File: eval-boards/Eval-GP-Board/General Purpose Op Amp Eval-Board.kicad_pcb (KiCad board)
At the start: 2 copper layers, 40 parts, among them J1 IN, J2 Conn_01x03_Male, J3 OUT, J4 TP1, J5 TP2, J6 TP3, J7 TP4, J8 TP5, J9 TP6, U1 ADA4522-1, U2 OPA847xD, U3 ADA4807-1

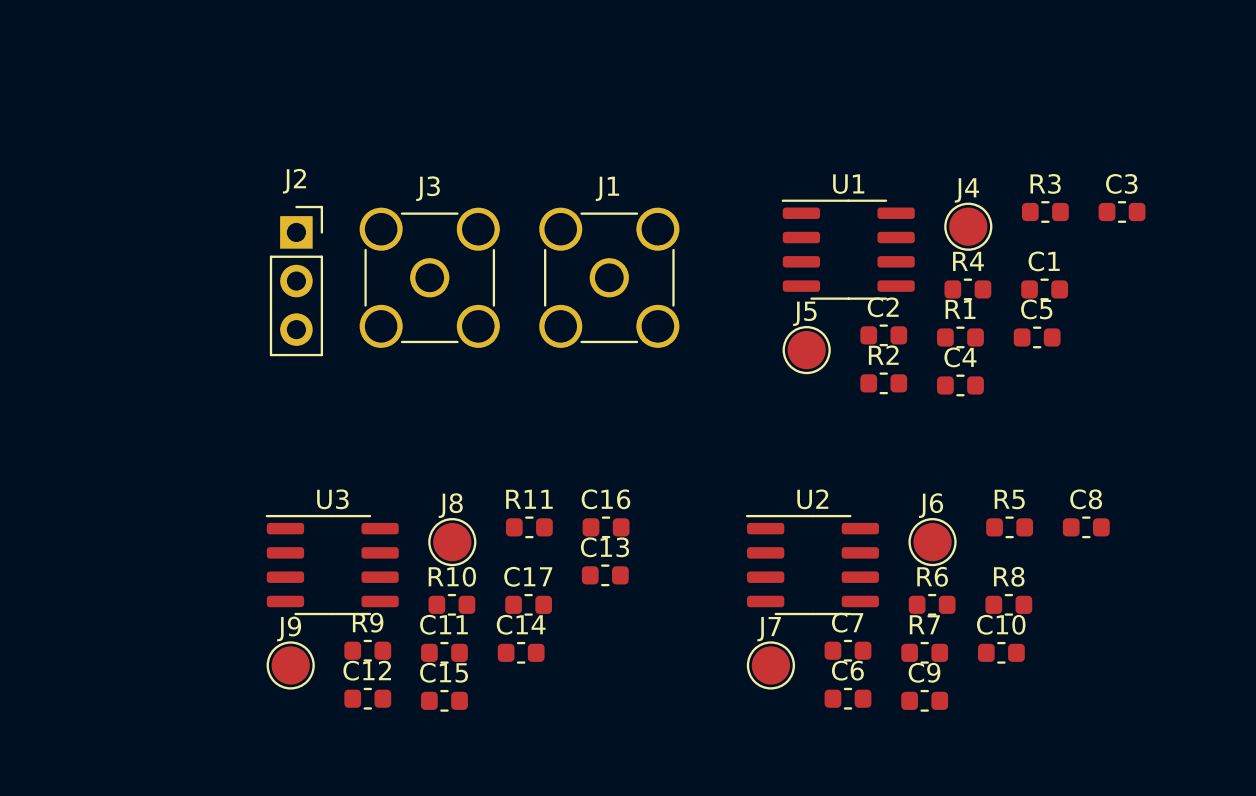
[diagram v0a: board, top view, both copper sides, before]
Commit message: Updated schematic
均采用双运放，前级4522可以单运放工作也可以级联工作
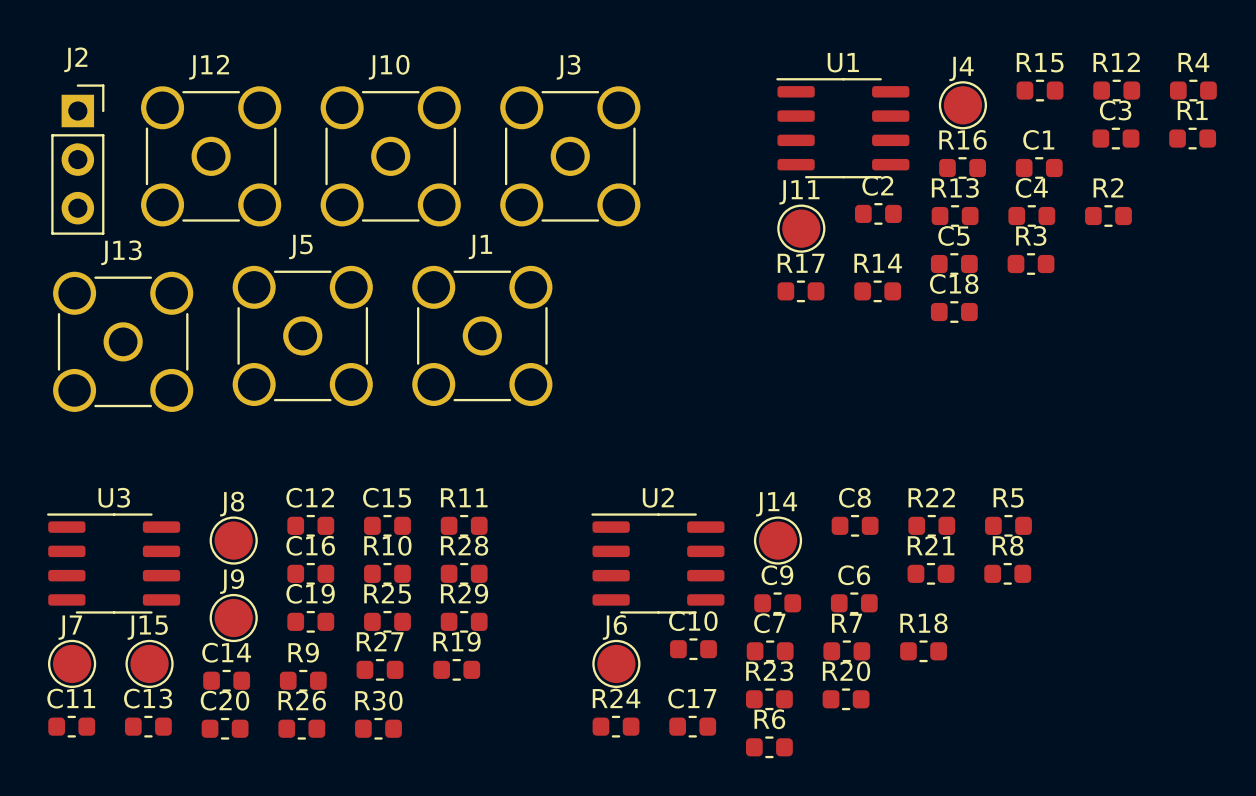
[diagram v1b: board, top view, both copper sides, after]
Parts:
- added C18: C, Capacitor_SMD:C_0603_1608Metric, F.Cu at (167.0, 98.7)
- added C19: C, Capacitor_SMD:C_0603_1608Metric, F.Cu at (133.4, 114.9)
- added C20: C, Capacitor_SMD:C_0603_1608Metric, F.Cu at (128.9, 120.5)
- added J10: OUT_B, Connector_Coaxial:SMA_Amphenol_901-144_Vertical, F.Cu at (137.6, 90.6)
- added J11: TP2, TestPoint:TestPoint_Pad_D2.0mm, F.Cu at (159.0, 94.3)
- added J12: IN_B, Connector_Coaxial:SMA_Amphenol_901-144_Vertical, F.Cu at (128.2, 90.6)
- added J13: OUT_B, Connector_Coaxial:SMA_Amphenol_901-144_Vertical, F.Cu at (123.6, 100.3)
- added J14: TP4, TestPoint:TestPoint_Pad_D2.0mm, F.Cu at (157.8, 110.6)
- added J15: TP8, TestPoint:TestPoint_Pad_D2.0mm, F.Cu at (125.0, 117.1)
- added R12: R, Resistor_SMD:R_0603_1608Metric, F.Cu at (175.5, 87.1)
- added R13: R, Resistor_SMD:R_0603_1608Metric, F.Cu at (167.1, 93.7)
- added R14: R, Resistor_SMD:R_0603_1608Metric, F.Cu at (163.0, 97.6)
- added R15: R, Resistor_SMD:R_0603_1608Metric, F.Cu at (171.5, 87.1)
- added R16: R, Resistor_SMD:R_0603_1608Metric, F.Cu at (167.5, 91.2)
- added R17: R, Resistor_SMD:R_0603_1608Metric, F.Cu at (159.0, 97.6)
- added R18: R, Resistor_SMD:R_0603_1608Metric, F.Cu at (165.4, 116.4)
- added R19: R, Resistor_SMD:R_0603_1608Metric, F.Cu at (141.0, 117.4)
- added R20: R, Resistor_SMD:R_0603_1608Metric, F.Cu at (161.4, 118.9)
- added R21: R, Resistor_SMD:R_0603_1608Metric, F.Cu at (165.8, 112.4)
- added R22: R, Resistor_SMD:R_0603_1608Metric, F.Cu at (165.9, 109.9)
- added R23: R, Resistor_SMD:R_0603_1608Metric, F.Cu at (157.4, 118.9)
- added R24: R, Resistor_SMD:R_0603_1608Metric, F.Cu at (149.3, 120.4)
- added R25: R, Resistor_SMD:R_0603_1608Metric, F.Cu at (137.4, 114.9)
- added R26: R, Resistor_SMD:R_0603_1608Metric, F.Cu at (132.9, 120.5)
- added R27: R, Resistor_SMD:R_0603_1608Metric, F.Cu at (137.0, 117.4)
- added R28: R, Resistor_SMD:R_0603_1608Metric, F.Cu at (141.4, 112.4)
- added R29: R, Resistor_SMD:R_0603_1608Metric, F.Cu at (141.4, 114.9)
- added R30: R, Resistor_SMD:R_0603_1608Metric, F.Cu at (136.9, 120.5)
- J1: value IN -> IN_A
- J3: value OUT -> OUT_A
- J5: value TP2 -> OUT_A; footprint TestPoint:TestPoint_Pad_D2.0mm -> Connector_Coaxial:SMA_Amphenol_901-144_Vertical
- J7: value TP4 -> TP6
- J9: value TP6 -> TP7
- U1: value ADA4522-1 -> ADA4522-2
- U2: value OPA847xD -> ADA4075-2
- U3: value ADA4807-1 -> ADA4807-2ARM
- moved J7 36.5 mm to (120.9, 117.1)
- moved J5 26.4 mm to (133.0, 99.9)
- moved C13 25.2 mm to (124.9, 120.4)
- moved C11 19.9 mm to (120.9, 120.4)
- moved J6 17.7 mm to (149.4, 117.1)
- moved C10 16.1 mm to (153.4, 116.3)
- moved R1 16.0 mm to (179.5, 89.6)
- moved R4 15.7 mm to (179.5, 87.1)
- moved C16 15.6 mm to (133.4, 112.4)
- moved C14 15.5 mm to (129.0, 118.0)
- moved R2 14.7 mm to (175.1, 93.7)
- moved J2 13.1 mm to (121.2, 88.2)
- moved C8 12.1 mm to (161.8, 109.9)
- moved J8 11.4 mm to (129.4, 110.6)
- moved U3 11.4 mm to (123.1, 111.8)
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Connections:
- net /Low noise amplifier/OUT renamed /Low noise amplifier/OUT_A
- C1 pad 1: /VEE -> /VCC
- C10 pad 1: /High gain amplifier/OUT -> /High gain amplifier/OUT_A
- C15 pad 1: /Second order filtering/OUT -> Net-(C15-Pad1)
- C17 pad 1: /Second order filtering/OUT -> /High gain amplifier/OUT_B
- C2 pad 1: /VEE -> /VCC
- C3 pad 1: /VCC -> /VEE
- C4 pad 1: /VCC -> /VEE
- J1 pad 1: /Low noise amplifier/signal_in -> /Low noise amplifier/signal_in_A
- J3 pad 1: /Second order filtering/OUT -> /Second order filtering/OUT_A
- J4 pad 1: /Low noise amplifier/signal_in -> /Low noise amplifier/signal_in_A
- J7 pad 1: /High gain amplifier/OUT -> /High gain amplifier/OUT_B
- J8 pad 1: /High gain amplifier/OUT -> /High gain amplifier/OUT_A
- J9 pad 1: /Second order filtering/OUT -> /Second order filtering/OUT_A
- R1 pad 1: /Low noise amplifier/signal_in -> Net-(R1-Pad1)
- R1 pad 2: GND -> Net-(R1-Pad2)
- R11 pad 1: /Second order filtering/OUT -> Net-(R11-Pad1)
- R11 pad 2: Net-(C17-Pad2) -> Net-(C15-Pad1)
- R2 pad 1: Net-(R2-Pad1) -> /Low noise amplifier/signal_in_A
- R2 pad 2: /Low noise amplifier/signal_in -> GND
- R3 pad 1: Net-(R2-Pad1) -> Net-(R3-Pad1)
- R3 pad 2: GND -> /Low noise amplifier/signal_in_A
- R4 pad 1: Net-(C5-Pad2) -> Net-(R3-Pad1)
- R4 pad 2: Net-(R4-Pad2) -> GND
- R6 pad 1: Net-(C10-Pad2) -> Net-(R18-Pad2)
- R9 pad 2: /High gain amplifier/OUT -> /High gain amplifier/OUT_A
- U1 pad 1: (no net) -> Net-(R1-Pad2)
- U1 pad 2: Net-(R4-Pad2) -> Net-(R1-Pad1)
- U1 pad 3: Net-(R2-Pad1) -> Net-(R3-Pad1)
- U1 pad 5: (no net) -> Net-(R13-Pad1)
- U1 pad 6: Net-(C5-Pad2) -> Net-(R17-Pad2)
- U1 pad 7: /VCC -> Net-(R14-Pad1)
- U1 pad 8: (no net) -> /VCC
- U2 pad 1: (no net) -> Net-(R18-Pad2)
- U2 pad 5: (no net) -> Net-(R21-Pad1)
- U2 pad 6: Net-(C10-Pad2) -> Net-(R23-Pad2)
- U2 pad 7: /VCC -> Net-(R23-Pad1)
- U2 pad 8: (no net) -> /VCC
- U3 pad 1: /Second order filtering/OUT -> Net-(C15-Pad1)
- U3 pad 2: /VEE -> Net-(R11-Pad1)
- U3 pad 4: Net-(C17-Pad2) -> /VEE
- U3 pad 5: (no net) -> Net-(C19-Pad1)
- U3 pad 6: /VCC -> Net-(R27-Pad1)
- U3 pad 7: (no net) -> Net-(C20-Pad1)
- U3 pad 8: (no net) -> /VCC

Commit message: first edition PCB
复杂度有点高。。。画的有点晕，问题很大
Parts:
- moved R2 120.9 mm to (55.9, 73.7), turned to 90 degrees
- moved R4 120.6 mm to (59.7, 73.7), turned to 90 degrees
- moved J4 117.2 mm to (52.1, 67.3)
- moved C1 113.8 mm to (57.6, 91.4)
- moved R1 113.0 mm to (67.3, 75.7), turned to 90 degrees
- moved C6 110.0 mm to (57.1, 80.0)
- moved C3 109.5 mm to (66.0, 86.4), turned to 180 degrees
- moved R12 109.4 mm to (67.3, 71.1), turned to 270 degrees
- moved R3 109.2 mm to (63.5, 77.5), turned to 180 degrees
- moved C4 106.8 mm to (64.8, 83.0), turned to 270 degrees
- moved C2 106.1 mm to (57.1, 87.6)
- moved C7 105.0 mm to (57.1, 85.1)
- moved C5 103.8 mm to (67.3, 67.3), turned to 270 degrees
- moved J1 99.4 mm to (52.1, 58.4)
- moved C8 97.1 mm to (66.0, 94.0), turned to 180 degrees
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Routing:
- net GND: track 0.00 -> 164.1 mm, vias 0 -> 2
- net /VCC: track 0.00 -> 119.7 mm, vias 0 -> 4
- net /VEE: track 0.00 -> 83.5 mm, vias 0 -> 4
- net /Low noise amplifier/OUT_A: track 0.00 -> 52.5 mm, vias 0 -> 4
- net /Low noise amplifier/signal_in_B: track 0.00 -> 45.1 mm, vias 0 -> 2
- net /Second order filtering/OUT_A: track 0.00 -> 42.0 mm, vias 0 -> 2
- net /Low noise amplifier/signal_in_A: track 0.00 -> 26.0 mm, vias 0 -> 2
- net /High gain amplifier/OUT_A: track 0.00 -> 24.9 mm, vias 0 -> 2
- net /Second order filtering/OUT_B: track 0.00 -> 20.1 mm
- net Net-(R11-Pad1): track 0.00 -> 18.2 mm
- net Net-(C14-Pad2): track 0.00 -> 18.1 mm, vias 0 -> 2
- net /High gain amplifier/OUT_B: track 0.00 -> 17.0 mm, vias 0 -> 2
- net Net-(C19-Pad1): track 0.00 -> 14.3 mm
- net Net-(C20-Pad2): track 0.00 -> 14.0 mm
- net Net-(C20-Pad1): track 0.00 -> 13.9 mm
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
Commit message: update-version
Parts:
- renumbered J1 to IN_A, J12 to IN_B, J3 to OUT_A, J5 to OUT_A, J10 to OUT_B, J13 to OUT_B, J4 to TP1, J11 to TP2, J6 to TP3, J14 to TP4, J8 to TP5, J7 to TP6, J9 to TP7, J15 to TP8
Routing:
- net /Second order filtering/OUT_A: track 42.0 -> 40.9 mm
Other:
- board outline added: 81.3 x 53.3 mm
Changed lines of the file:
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@@
   (general
     (thickness 1.6)
-    (drawings 4)
-    (tracks 297)
+    (drawings 8)
+    (tracks 298)
     (zones 0)
     (modules 68)
@@
   )
   (setup
-    (last_trace_width 0.4)
+    (last_trace_width 0.25)
     (user_trace_width 0.4)
     (trace_clearance 0.2)
@@
     (tags capacitor)
     (attr smd)
-    (fp_text reference C9 (at 0 -1.43) (layer F.SilkS)
+    (fp_text reference C9 (at 0 -1.27) (layer F.SilkS)
       (effects (font (size 1 1) (thickness 0.15)))
     )
@@
     (tags capacitor)
     (attr smd)
-    (fp_text reference C13 (at 0 -1.43) (layer F.SilkS)
+    (fp_text reference C13 (at 0 1.27) (layer F.SilkS)
       (effects (font (size 1 1) (thickness 0.15)))
     )
@@
     (descr https://www.amphenolrf.com/downloads/dl/file/id/7023/product/3103/901_144_customer_drawing.pdf)
     (tags "SMA THT Female Jack Vertical")
-    (fp_text reference J1 (at 0 -4.75) (layer F.SilkS)
+    (fp_text reference IN_A (at 0 -5.08) (layer F.SilkS)
       (effects (font (size 1 1) (thickness 0.15)))
     )
@@
     (descr https://www.amphenolrf.com/downloads/dl/file/id/7023/product/3103/901_144_customer_drawing.pdf)
     (tags "SMA THT Female Jack Vertical")
-    (fp_text reference J3 (at 0 -4.75) (layer F.SilkS)
+    (fp_text reference OUT_A (at 0 -4.75) (layer F.SilkS)
       (effects (font (size 1 1) (thickness 0.15)))
     )
@@
     (tags "test point SMD pad")
     (attr virtual)
-    (fp_text reference J4 (at 0 -1.998) (layer F.SilkS)
+    (fp_text reference TP1 (at -3.81 0) (layer F.SilkS)
       (effects (font (size 1 1) (thickness 0.15)))
     )
@@
     (fp_circle (center 0 0) (end 0 1.2) (layer F.SilkS) (width 0.12))
     (fp_circle (center 0 0) (end 1.5 0) (layer F.CrtYd) (width 0.05))
-    (fp_text user %R (at 0 -2) (layer F.Fab)
-      (effects (font (size 1 1) (thickness 0.15)))
-    )
     (pad 1 smd circle (at 0 0) (size 2 2) (layers F.Cu F.Mask)
       (net 20 "/Low noise amplifier/signal_in_A"))
@@
     (descr https://www.amphenolrf.com/downloads/dl/file/id/7023/product/3103/901_144_customer_drawing.pdf)
     (tags "SMA THT Female Jack Vertical")
-    (fp_text reference J5 (at 0 -4.75) (layer F.SilkS)
+    (fp_text reference OUT_A (at 0 -4.75) (layer F.SilkS)
       (effects (font (size 1 1) (thickness 0.15)))
     )
@@
     (tags "test point SMD pad")
     (attr virtual)
-    (fp_text reference J6 (at 0 -1.998) (layer F.SilkS)
+    (fp_text reference TP3 (at 0 -1.998) (layer F.SilkS)
       (effects (font (size 1 1) (thickness 0.15)))
     )
@@
     (tags "test point SMD pad")
     (attr virtual)
-    (fp_text reference J7 (at 0 -1.998) (layer F.SilkS)
+    (fp_text reference TP6 (at 2.54 0) (layer F.SilkS)
       (effects (font (size 1 1) (thickness 0.15)))
     )
@@
     (tags "test point SMD pad")
     (attr virtual)
-    (fp_text reference J8 (at 0 -1.998) (layer F.SilkS)
+    (fp_text reference TP5 (at 0 -1.998) (layer F.SilkS)
       (effects (font (size 1 1) (thickness 0.15)))
     )
@@
     (tags "test point SMD pad")
     (attr virtual)
-    (fp_text reference J9 (at 0 -1.998) (layer F.SilkS)
+    (fp_text reference TP7 (at 0 -1.998) (layer F.SilkS)
       (effects (font (size 1 1) (thickness 0.15)))
     )
@@
     (descr https://www.amphenolrf.com/downloads/dl/file/id/7023/product/3103/901_144_customer_drawing.pdf)
     (tags "SMA THT Female Jack Vertical")
-    (fp_text reference J10 (at 0 -4.75) (layer F.SilkS)
+    (fp_text reference OUT_B (at 0 -4.75) (layer F.SilkS)
       (effects (font (size 1 1) (thickness 0.15)))
     )
@@
     (tags "test point SMD pad")
     (attr virtual)
-    (fp_text reference J11 (at 0 -1.998) (layer F.SilkS)
+    (fp_text reference TP2 (at 0 -1.998) (layer F.SilkS)
       (effects (font (size 1 1) (thickness 0.15)))
     )
@@
     (descr https://www.amphenolrf.com/downloads/dl/file/id/7023/product/3103/901_144_customer_drawing.pdf)
     (tags "SMA THT Female Jack Vertical")
-    (fp_text reference J12 (at 0 -4.75) (layer F.SilkS)
+    (fp_text reference IN_B (at 0 -4.75) (layer F.SilkS)
       (effects (font (size 1 1) (thickness 0.15)))
     )
@@
     (descr https://www.amphenolrf.com/downloads/dl/file/id/7023/product/3103/901_144_customer_drawing.pdf)
     (tags "SMA THT Female Jack Vertical")
-    (fp_text reference J13 (at 0 -4.75) (layer F.SilkS)
+    (fp_text reference OUT_B (at 0 -4.75) (layer F.SilkS)
       (effects (font (size 1 1) (thickness 0.15)))
     )
@@
     (tags "test point SMD pad")
     (attr virtual)
-    (fp_text reference J14 (at 0 -1.998) (layer F.SilkS)
-      (effects (font (size 1 1) (thickness 0.15)))
-    )
-    (fp_text value TP4 (at 0 2.05) (layer F.Fab)
-      (effects (font (size 1 1) (thickness 0.15)))
-    )
-    (fp_text user %R (at 0 -2) (layer F.Fab)
+    (fp_text reference TP4 (at 0 2.54) (layer F.SilkS)
+      (effects (font (size 1 1) (thickness 0.15)))
+    )
+    (fp_text value TP4 (at 0 -2.54) (layer F.Fab)
       (effects (font (size 1 1) (thickness 0.15)))
     )
@@
     (tags "test point SMD pad")
     (attr virtual)
-    (fp_text reference J15 (at 0 -1.998) (layer F.SilkS)
+    (fp_text reference TP8 (at 2.54 0) (layer F.SilkS)
       (effects (font (size 1 1) (thickness 0.15)))
     )
@@
     (tags resistor)
     (attr smd)
-    (fp_text reference R29 (at 0 -1.43) (layer F.SilkS)
+    (fp_text reference R29 (at 0 1.27) (layer F.SilkS)
       (effects (font (size 1 1) (thickness 0.15)))
     )
@@
     )
   )
+  (gr_line (start 127 52.07) (end 45.72 52.07) (layer Edge.Cuts) (width 0.05))
+  (gr_line (start 127 105.41) (end 127 52.07) (layer Edge.Cuts) (width 0.05))
+  (gr_line (start 45.72 105.41) (end 127 105.41) (layer Edge.Cuts) (width 0.05))
+  (gr_line (start 45.72 52.07) (end 45.72 105.41) (layer Edge.Cuts) (width 0.05))
   (gr_line (start 127 52.07) (end 45.72 52.07) (layer F.SilkS) (width 0.12))
   (gr_line (start 127 105.41) (end 127 52.07) (layer F.SilkS) (width 0.12))
@@
   (segment (start 113.03 81.28) (end 113.03 64.77) (width 0.4) (layer B.Cu) (net 21))
   (segment (start 116.84 60.96) (end 119.38 60.96) (width 0.4) (layer F.Cu) (net 21))
-  (segment (start 113.03 64.77) (end 116.84 60.96) (width 0.4) (layer F.Cu) (net 21))
   (segment (start 114.3 60.96) (end 119.38 60.96) (width 0.4) (layer F.Cu) (net 21))
   (segment (start 113.03 59.69) (end 114.3 60.96) (width 0.4) (layer F.Cu) (net 21))
+  (segment (start 114.3 60.96) (end 114.3 63.5) (width 0.25) (layer F.Cu) (net 21))
+  (segment (start 114.3 63.5) (end 113.03 64.77) (width 0.25) (layer F.Cu) (net 21))
   (segment (start 84.6075 85.09) (end 82.0675 85.09) (width 0.4) (layer F.Cu) (net 22))
   (segment (start 87.63 82.0675) (end 84.6075 85.09) (width 0.4) (layer F.Cu) (net 22))
